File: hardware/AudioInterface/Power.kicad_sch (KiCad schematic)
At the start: 12 parts, among them SW1 RST, U6 TLV75533PDRV, U7 APX811-40UG-7, U8 TLV73312PDRV, U9 LP5910-1.8DRV

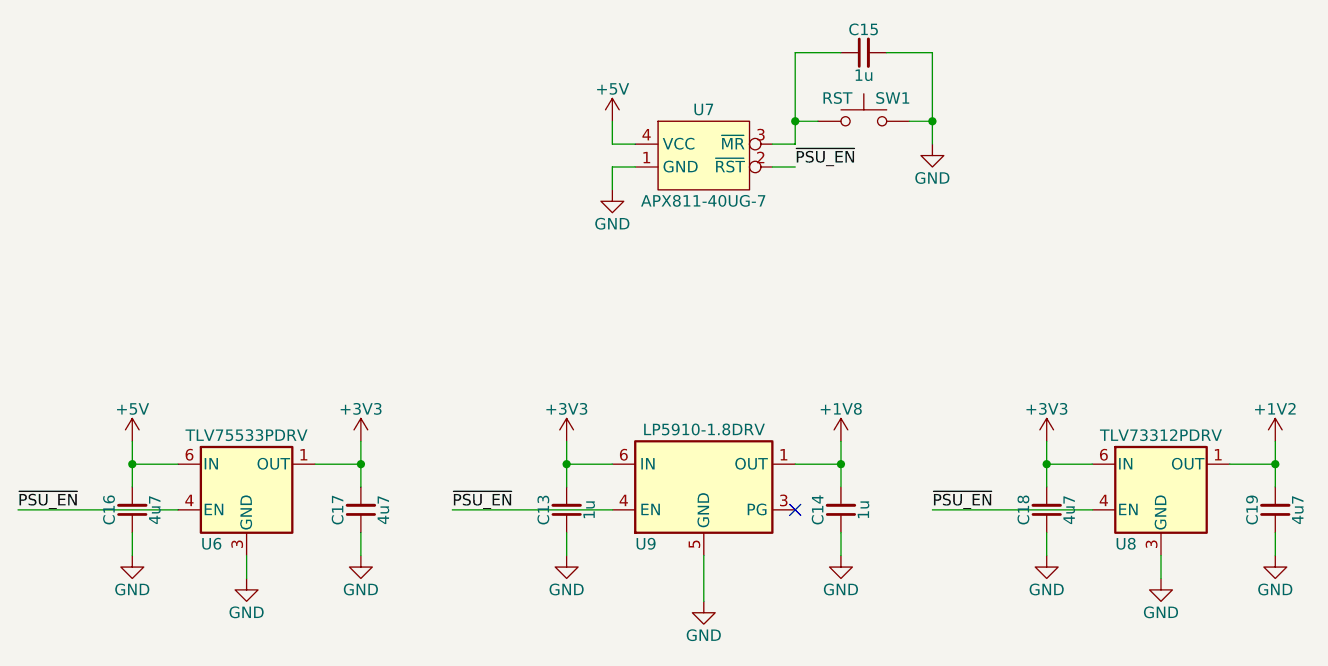
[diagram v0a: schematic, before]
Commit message: Improved the PSU enable/reset handling on the audio interface board
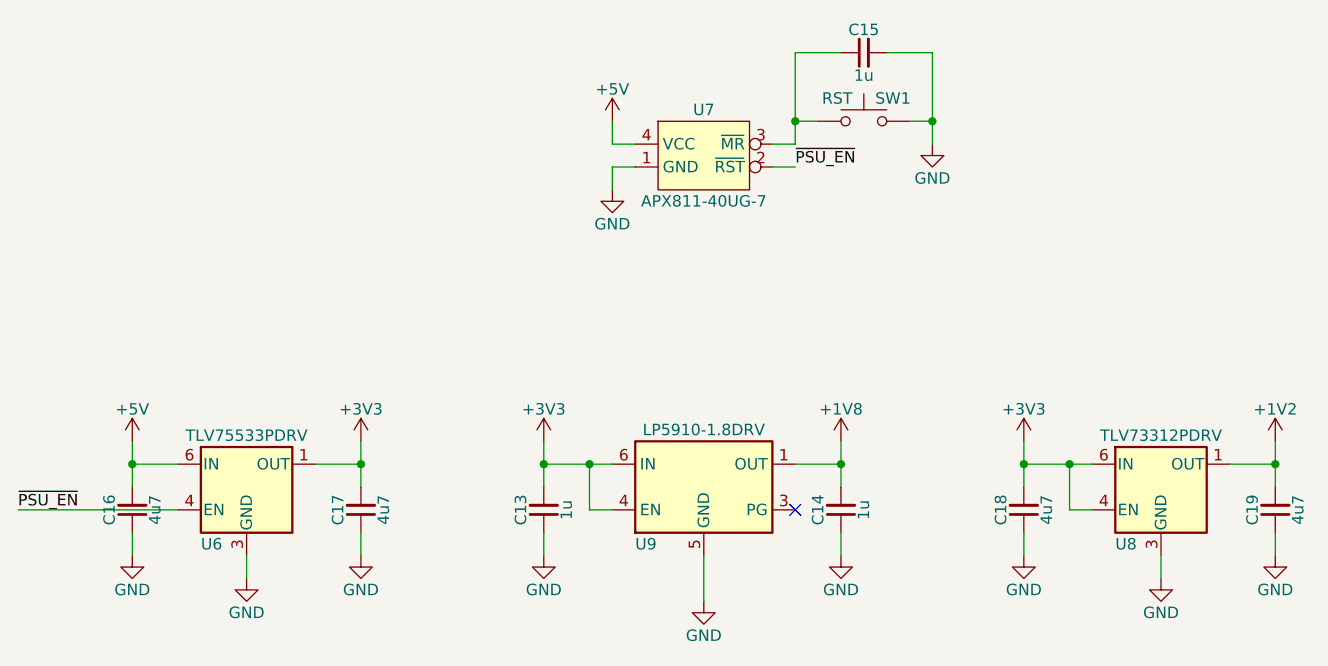
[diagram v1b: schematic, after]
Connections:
- net +3V3: now also U8.4 (EN), U9.4 (EN)
- net ~{PSU_EN}: no longer U8.4 (EN), U9.4 (EN)
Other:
- moved on the sheet: C13, C18

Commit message: Completed a pile more work on the various boards that comprise the project
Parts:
- C13, C14, C15: MFR (none) -> Kemet; MPN (none) -> C0603C105K4RAC7867; OC_DIGIKEY (none) -> 399-C0603C105K4RAC7867CT-ND; URL_DIGIKEY (none) -> https://www.digikey.com/en/products/detail/kemet/C0603C105K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
- C16, C17, C18, C19: MFR (none) -> TDK; MPN (none) -> C1608X5R1C475K080AC; OC_DIGIKEY (none) -> 445-7478-1-ND; URL_DIGIKEY (none) -> https://www.digikey.com/en/products/detail/tdk-corporation/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
- SW1: MFR (none) -> Omron; MPN (none) -> B3U-1000P-B; OC_DIGIKEY (none) -> SW1143CT-ND; URL_DIGIKEY (none) -> https://www.digikey.com/en/products/detail/omron-electronic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
- U6: MPN (none) -> TLV75533PDRVR; OC_DIGIKEY (none) -> 296-51807-1-ND; URL_DIGIKEY (none) -> https://www.digikey.com/en/products/detail/texas-instrument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
- U7: OC_DIGIKEY (none) -> APX811-40UG-7CT-ND; URL_DIGIKEY (none) -> https://www.digikey.com/en/products/detail/diodes-incorpora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
- U8: MPN (none) -> TLV73312PQDRVRQ1; OC_DIGIKEY (none) -> 296-44834-1-ND; URL_DIGIKEY (none) -> https://www.digikey.com/en/products/detail/texas-instrument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
- U9: MPN (none) -> LP5910-1.8DRVR; OC_DIGIKEY (none) -> 296-47212-1-ND; URL_DIGIKEY (none) -> https://www.digikey.com/en/products/detail/texas-instrument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
